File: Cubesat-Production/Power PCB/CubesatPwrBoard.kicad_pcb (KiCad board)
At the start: 2 copper layers, 90 x 96 mm, 57 parts, among them J1 SystemLoad, J10 Test_Point, J11 Test_Point, J14 Test_Point, J15 Test_Point, J16 Test_Point_GND, J2 SystemLoad, J3 I2C, J6 Test_Point, J7 Test_Point, Q1 TQM110NB04CR_RLG, Q2 2N7002*, U1 LTC4162

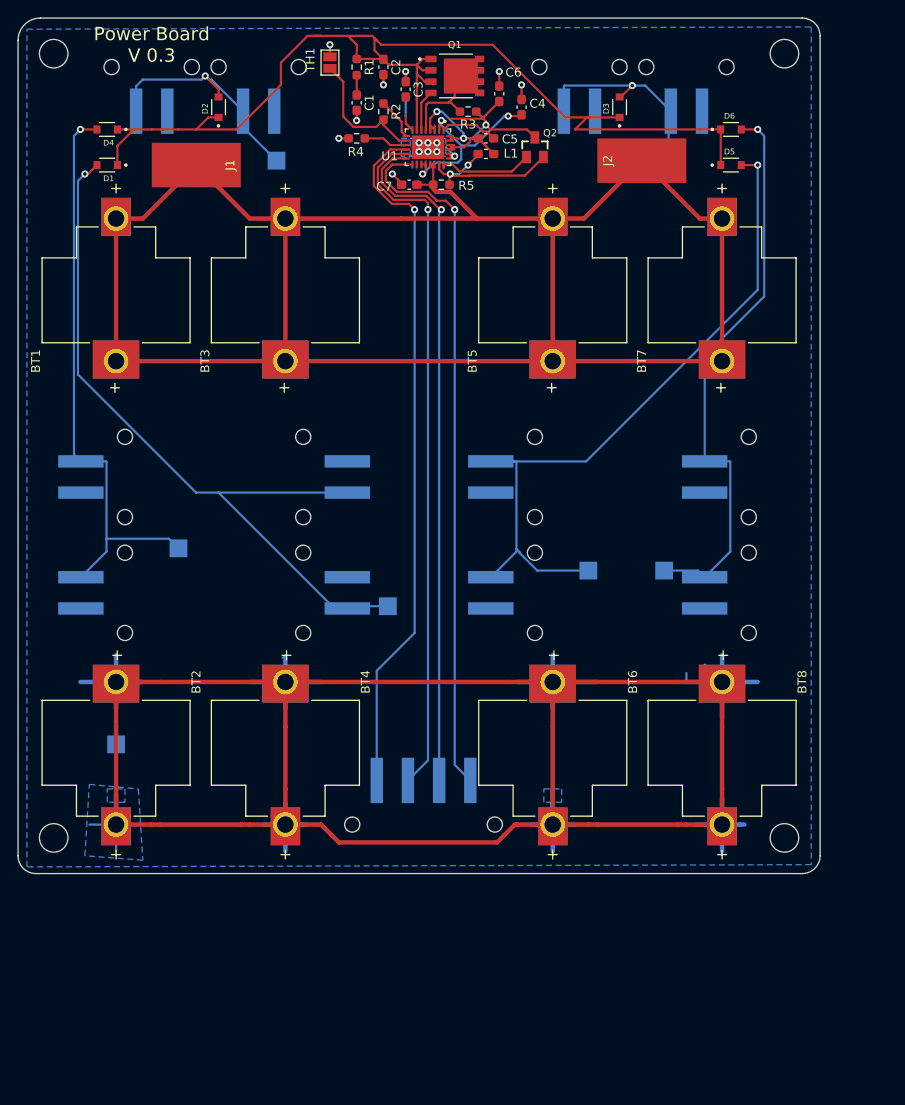
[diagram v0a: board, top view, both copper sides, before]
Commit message: copies current-revision to production branch
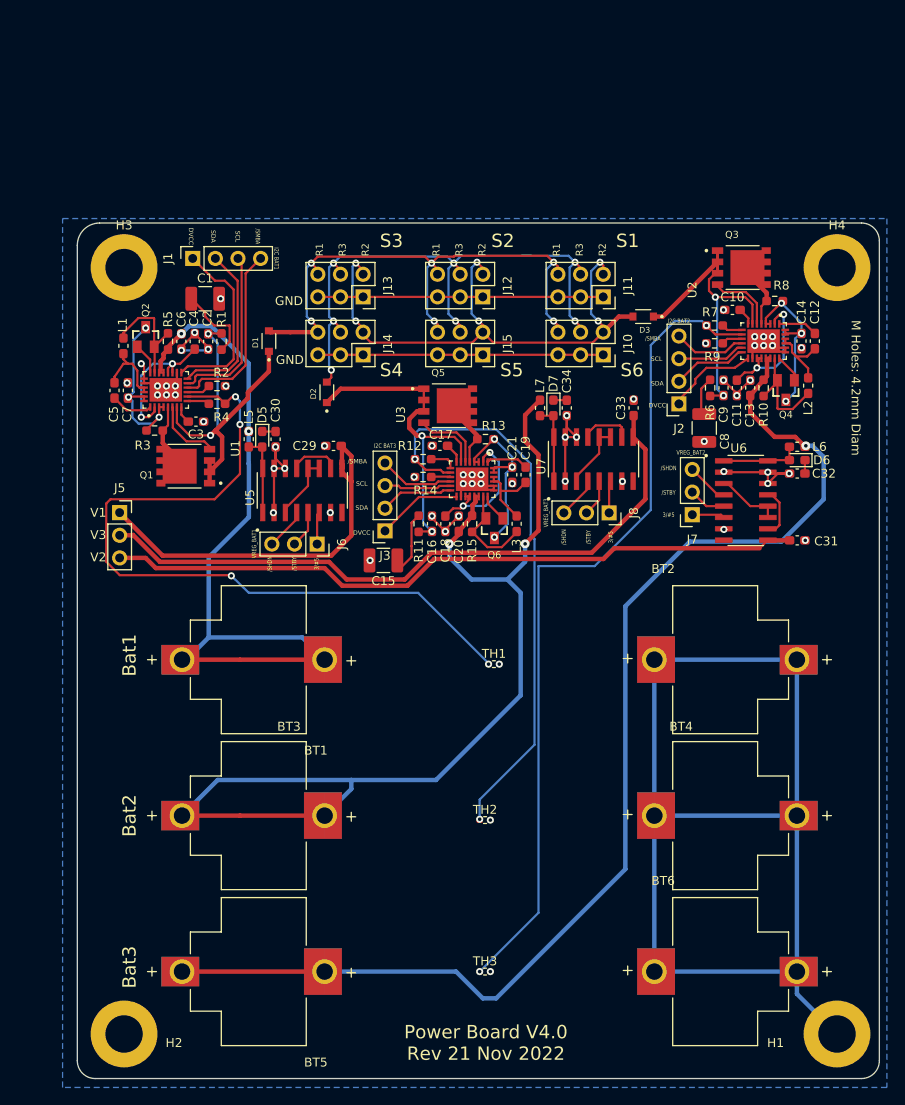
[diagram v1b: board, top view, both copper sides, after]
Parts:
- removed BT7, BT8: 254TR, 254TR:BAT_254TR
- removed D4: D_Schottky_Small, CUS520,H3F:DIO_CUS520,H3F
- removed J16: Test_Point_GND, TestPoint:TestPoint_Pad_2.0x2.0mm
- removed REF** (x4): MountingHole_3.2mm_M3, MountingHole:MountingHole_3.2mm_M3
- removed SC1, SC10, SC11, SC12, SC2, SC3, SC4, SC5, SC6, SC7, SC8, SC9: Solar_Cells, 6915_1x2:691508110302
- added C10: 1u, Capacitor_SMD:C_0603_1608Metric_Pad1.08x0.95mm_HandSolder, F.Cu at (180.2, 55.2)
- added C11: 4.7u, Capacitor_SMD:C_0603_1608Metric_Pad1.08x0.95mm_HandSolder, F.Cu at (180.7, 64.0)
- added C12: C, Capacitor_SMD:C_0603_1608Metric_Pad1.08x0.95mm_HandSolder, F.Cu at (189.4, 58.8)
- added C13: 10u, Capacitor_SMD:C_0603_1608Metric_Pad1.08x0.95mm_HandSolder, F.Cu at (182.2, 64.0)
- added C14: 10u, Capacitor_SMD:C_0603_1608Metric_Pad1.08x0.95mm_HandSolder, F.Cu at (187.9, 58.8)
- added C15: 150u, Capacitor_SMD:C_1210_3225Metric_Pad1.33x2.70mm_HandSolder, F.Cu at (141.0, 83.4)
- added C16: C_Polarized_US, Capacitor_SMD:C_0603_1608Metric_Pad1.08x0.95mm_HandSolder, F.Cu at (146.5, 79.2)
- added C17: 1u, Capacitor_SMD:C_0603_1608Metric_Pad1.08x0.95mm_HandSolder, F.Cu at (147.3, 70.5)
- added C18: 4.7u, Capacitor_SMD:C_0603_1608Metric_Pad1.08x0.95mm_HandSolder, F.Cu at (148.0, 79.2)
- added C19: C, Capacitor_SMD:C_0603_1608Metric_Pad1.08x0.95mm_HandSolder, F.Cu at (157.0, 73.8)
- added C20: 10u, Capacitor_SMD:C_0603_1608Metric_Pad1.08x0.95mm_HandSolder, F.Cu at (149.5, 79.2)
- added C21: 10u, Capacitor_SMD:C_0603_1608Metric_Pad1.08x0.95mm_HandSolder, F.Cu at (155.5, 73.8)
- added C29: C_Polarized_US, Capacitor_SMD:C_0603_1608Metric_Pad1.08x0.95mm_HandSolder, F.Cu at (135.4, 70.5)
- added C30: C_Polarized_US, Capacitor_SMD:C_0603_1608Metric_Pad1.08x0.95mm_HandSolder, F.Cu at (128.9, 69.8)
- added C31: 4.7u, Capacitor_SMD:C_0603_1608Metric_Pad1.08x0.95mm_HandSolder, F.Cu at (187.4, 81.1)
- added C32: 100u, Capacitor_SMD:C_0603_1608Metric_Pad1.08x0.95mm_HandSolder, F.Cu at (187.4, 73.6)
- added C33: 4.7u, Capacitor_SMD:C_0603_1608Metric_Pad1.08x0.95mm_HandSolder, F.Cu at (169.1, 66.2)
- added C34: 100u, Capacitor_SMD:C_0603_1608Metric_Pad1.08x0.95mm_HandSolder, F.Cu at (161.6, 66.2)
- added C8: 150u, Capacitor_SMD:C_1210_3225Metric_Pad1.33x2.70mm_HandSolder, F.Cu at (177.0, 68.5)
- added C9: C_Polarized_US, Capacitor_SMD:C_0603_1608Metric_Pad1.08x0.95mm_HandSolder, F.Cu at (179.2, 64.0)
- added D7: D_Schottky, Diode_SMD:D_0603_1608Metric_Pad1.05x0.95mm_HandSolder, F.Cu at (160.1, 66.2)
- added H1: MountingHole_Pad, MountingHole:MountingHole_4.3mm_M4_DIN965_Pad, F.Cu at (191.9, 136.5)
- added H2: MountingHole_Pad, MountingHole:MountingHole_4.3mm_M4_DIN965_Pad, F.Cu at (111.9, 136.5)
- added H3: MountingHole_Pad, MountingHole:MountingHole_4.3mm_M4_DIN965_Pad, F.Cu at (111.9, 50.5)
- added H4: MountingHole_Pad, MountingHole:MountingHole_4.3mm_M4_DIN965_Pad, F.Cu at (191.9, 50.5)
- added J12: S3, Connector_PinSocket_2.54mm:PinSocket_2x03_P2.54mm_Vertical, F.Cu at (152.2, 53.8)
- added J13: S4, Connector_PinSocket_2.54mm:PinSocket_2x03_P2.54mm_Vertical, F.Cu at (138.7, 53.8)
- added J5: Conn_01x04_Female, Connector_PinSocket_2.54mm:PinSocket_1x03_P2.54mm_Vertical, F.Cu at (111.4, 78.0)
- added J8: Conn_01x03_Female, Connector_PinSocket_2.54mm:PinSocket_1x03_P2.54mm_Vertical, F.Cu at (166.3, 78.0)
- added L2: 4.7u, Inductor_SMD:L_0603_1608Metric_Pad1.05x0.95mm_HandSolder, F.Cu at (188.7, 63.8)
- added L3: 4.7u, Inductor_SMD:L_0603_1608Metric_Pad1.05x0.95mm_HandSolder, F.Cu at (156.0, 79.2)
- added L5: L, Inductor_SMD:L_0603_1608Metric_Pad1.05x0.95mm_HandSolder, F.Cu at (125.9, 69.8)
- added L6: 22u, Inductor_SMD:L_0603_1608Metric_Pad1.05x0.95mm_HandSolder, F.Cu at (187.4, 70.6)
- added L7: 22u, Inductor_SMD:L_0603_1608Metric_Pad1.05x0.95mm_HandSolder, F.Cu at (158.6, 66.2)
- added Q3: TQM110NB04CR_RLG, TQM110N:TRANS_TQM110NB04CR_RLG, F.Cu at (181.2, 50.5)
- added Q4: 2N7002*, 2N7002:SOT23, F.Cu at (186.2, 64.2)
- added Q5: TQM110NB04CR_RLG, TQM110N:TRANS_TQM110NB04CR_RLG, F.Cu at (148.2, 66.0)
- added Q6: 2N7002*, 2N7002:SOT23, F.Cu at (153.5, 79.8)
- added R10: 10m, Resistor_SMD:R_0603_1608Metric_Pad0.98x0.95mm_HandSolder, F.Cu at (183.7, 64.0)
- added R11: 2.5, Resistor_SMD:R_0603_1608Metric_Pad0.98x0.95mm_HandSolder, F.Cu at (145.0, 79.2)
- added R12: 16m, Resistor_SMD:R_0603_1608Metric_Pad0.98x0.95mm_HandSolder, F.Cu at (145.5, 72.0)
- added R13: 16m, Resistor_SMD:R_0603_1608Metric_Pad0.98x0.95mm_HandSolder, F.Cu at (152.5, 69.8)
- added R14: 63.4k, Resistor_SMD:R_0603_1608Metric_Pad0.98x0.95mm_HandSolder, F.Cu at (145.5, 74.0)
- added R15: 10m, Resistor_SMD:R_0603_1608Metric_Pad0.98x0.95mm_HandSolder, F.Cu at (151.0, 79.2)
- added R6: 2.5, Resistor_SMD:R_0603_1608Metric_Pad0.98x0.95mm_HandSolder, F.Cu at (177.7, 64.0)
- added R7: 16m, Resistor_SMD:R_0603_1608Metric_Pad0.98x0.95mm_HandSolder, F.Cu at (178.2, 57.0)
- added R8: 16m, Resistor_SMD:R_0603_1608Metric_Pad0.98x0.95mm_HandSolder, F.Cu at (184.9, 54.2)
- added R9: 63.4k, Resistor_SMD:R_0603_1608Metric_Pad0.98x0.95mm_HandSolder, F.Cu at (178.2, 59.0)
- added TH2: Thermistor_NTC, Resistor_SMD:R_0402_1005Metric_Pad0.72x0.64mm_HandSolder, F.Cu at (152.4, 112.5)
- added TH3: Thermistor_NTC, Resistor_SMD:R_0402_1005Metric_Pad0.72x0.64mm_HandSolder, F.Cu at (152.4, 129.5)
- added U2: LTC4162, LTC4162:QFN50P500X400X80-29N, F.Cu at (183.7, 58.8)
- added U3: LTC4162, LTC4162:QFN50P500X400X80-29N, F.Cu at (151.0, 74.2)
- added U5: MAX710ESE+T, MAX710ESE:SOIC127P600X175-16N, F.Cu at (131.9, 75.5)
- added U6: MAX710ESE+T, MAX710ESE:SOIC127P600X175-16N, F.Cu at (181.7, 76.6)
- added U7: MAX710ESE+T, MAX710ESE:SOIC127P600X175-16N, F.Cu at (164.6, 72.0)
- C1: value 150u -> C_Polarized_US; footprint Capacitor_SMD:C_0603_1608Metric_Pad1.08x0.95mm_HandSolder -> Capacitor_SMD:C_1210_3225Metric_Pad1.33x2.70mm_HandSolder
- C2: value 0.1u -> C_Polarized_US
- C3: value 1u -> C
- C4: value 4.7u -> C
- C5: value 22n -> C
- C6, C7: value 10u -> C
- D5, D6: value D_Schottky_Small -> D_Schottky; footprint CUS520,H3F:DIO_CUS520,H3F -> Diode_SMD:D_0603_1608Metric_Pad1.05x0.95mm_HandSolder
- J1, J2: value SystemLoad -> Conn_01x04_Female; footprint Connector_Wire:SolderWirePad_1x01_SMD_5x10mm -> Connector_PinSocket_2.54mm:PinSocket_1x04_P2.54mm_Vertical
- J10: value Test_Point -> S1; footprint TestPoint:TestPoint_Pad_2.0x2.0mm -> Connector_PinSocket_2.54mm:PinSocket_2x03_P2.54mm_Vertical; moved to F.Cu
- J11: value Test_Point -> S2; footprint TestPoint:TestPoint_Pad_2.0x2.0mm -> Connector_PinSocket_2.54mm:PinSocket_2x03_P2.54mm_Vertical; moved to F.Cu
- J14: value Test_Point -> S5; footprint TestPoint:TestPoint_Pad_2.0x2.0mm -> Connector_PinSocket_2.54mm:PinSocket_2x03_P2.54mm_Vertical; moved to F.Cu
- J15: value Test_Point -> S6; footprint TestPoint:TestPoint_Pad_2.0x2.0mm -> Connector_PinSocket_2.54mm:PinSocket_2x03_P2.54mm_Vertical; moved to F.Cu
- J3: value I2C -> Conn_01x04_Female; footprint 6915_1x4:691508110304 -> Connector_PinSocket_2.54mm:PinSocket_1x04_P2.54mm_Vertical; moved to F.Cu
- J6, J7: value Test_Point -> Conn_01x03_Female; footprint TestPoint:TestPoint_Pad_2.0x2.0mm -> Connector_PinSocket_2.54mm:PinSocket_1x03_P2.54mm_Vertical; moved to F.Cu
- L1: value 4.7u -> L
- R1: value 2.5 -> R
- R2, R3: value 16m -> R
- R4: value 63.4k -> R
- R5: value 10m -> R
- TH1: footprint Jumper:SolderJumper-2_P1.3mm_Open_Pad1.0x1.5mm -> Resistor_SMD:R_0402_1005Metric_Pad0.72x0.64mm_HandSolder
- moved BT5 83.6 mm to (126.4, 129.5), turned to 180 degrees
- moved TH1 70.0 mm to (153.4, 95.0), turned to 0 degrees
- moved BT2 69.2 mm to (179.4, 94.5), turned to 0 degrees
- moved J7 61.3 mm to (175.7, 78.2), turned to 180 degrees
- moved D5 60.9 mm to (127.4, 69.8), turned to -90 degrees
- moved BT3 59.1 mm to (126.4, 112.0), turned to 180 degrees
- moved J11 55.4 mm to (165.7, 53.8), turned to -90 degrees
- moved Q1 53.2 mm to (118.8, 72.8), turned to 180 degrees
- moved C5 50.4 mm to (110.8, 64.3), turned to 90 degrees
- moved R3 50.2 mm to (115.3, 68.8), turned to 0 degrees
- moved BT4 49.9 mm to (179.4, 112.0), turned to 0 degrees
- moved Q2 48.6 mm to (114.3, 58.3)
- moved L1 46.0 mm to (111.8, 59.3), turned to 90 degrees
- moved C6 45.2 mm to (118.3, 58.8), turned to -90 degrees
- moved C4 45.1 mm to (119.8, 58.8)
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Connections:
- net Net-(R2-Pad2) renamed /Bat_Reg_1/TH
- BT1 pad P1_1: Net-(BT1-PadP1_1) -> /Bat_Reg_1/V_Bat
- BT1 pad P1_2: Net-(BT1-PadP1_1) -> /Bat_Reg_1/V_Bat
- BT3 pad P1_1: Net-(BT1-PadP1_1) -> /Bat_Reg_2/V_Bat
- BT3 pad P1_2: Net-(BT1-PadP1_1) -> /Bat_Reg_2/V_Bat
- BT5 pad P1_1: Net-(BT1-PadP1_1) -> /Bat_Reg_3/V_Bat
- BT5 pad P1_2: Net-(BT1-PadP1_1) -> /Bat_Reg_3/V_Bat
- C2 pad 1: Net-(C2-Pad1) -> /Bat_Reg_1/VIN
- C6 pad 1: Net-(C6-Pad1) -> /Bat_Reg_1/V_Bat
- C7 pad 1: Net-(BT1-PadP1_1) -> Net-(C7-Pad1)
- D1 pad 1: Net-(C2-Pad1) -> /Bat_Reg_1/VIN
- D2 pad 1: Net-(C2-Pad1) -> /Bat_Reg_2/VIN
- D3 pad 1: Net-(C2-Pad1) -> /Bat_Reg_3/VIN
- D5 pad 1: Net-(C2-Pad1) -> Net-(C30-Pad1)
- D6 pad 1: Net-(C2-Pad1) -> Net-(C32-Pad1)
- J1 pad 1: Net-(BT1-PadP1_1) -> /Bat_Reg_1/DVCC
- J10 pad 1: Net-(D3-Pad2) -> GND
- J11 pad 1: Net-(D4-Pad2) -> GND
- J14 pad 1: Net-(D5-Pad2) -> GND
- J15 pad 1: Net-(D6-Pad2) -> GND
- J2 pad 1: Net-(BT1-PadP1_1) -> /Bat_Reg_3/DVCC
- J3 pad 1: Net-(J3-Pad1) -> /Bat_Reg_2/DVCC
- J3 pad 2: Net-(J3-Pad2) -> /Bat_Reg_2/SDA
- J3 pad 3: Net-(J3-Pad3) -> /Bat_Reg_2/SCL
- J3 pad 4: Net-(J3-Pad4) -> /Bat_Reg_2//SMBALERT
- J6 pad 1: Net-(D1-Pad2) -> /V_Reg_3.3_5V1/3/#5
- J7 pad 1: Net-(D2-Pad2) -> /V_Reg_3.3_5V3/3/#5
- Q1 pad 1: Net-(C2-Pad1) -> /Bat_Reg_1/VIN
- Q1 pad 2: Net-(C2-Pad1) -> /Bat_Reg_1/VIN
- Q1 pad 3: Net-(C2-Pad1) -> /Bat_Reg_1/VIN
- Q2 pad 3: Net-(C6-Pad1) -> Net-(C7-Pad1)
- R1 pad 1: Net-(C2-Pad1) -> /Bat_Reg_1/VIN
- R3 pad 1: Net-(C6-Pad1) -> Net-(C7-Pad1)
- R5 pad 1: Net-(BT1-PadP1_1) -> /Bat_Reg_1/V_Bat
- U1 pad 12: Net-(J3-Pad4) -> /Bat_Reg_1//SMBALERT
- U1 pad 13: Net-(J3-Pad3) -> /Bat_Reg_1/SCL
- U1 pad 14: Net-(J3-Pad2) -> /Bat_Reg_1/SDA
- U1 pad 15: Net-(J3-Pad1) -> /Bat_Reg_1/DVCC
- U1 pad 19: Net-(BT1-PadP1_1) -> /Bat_Reg_1/V_Bat
- U1 pad 20: Net-(BT1-PadP1_1) -> /Bat_Reg_1/V_Bat
- U1 pad 27: Net-(C6-Pad1) -> Net-(C7-Pad1)
- U1 pad 28: Net-(C6-Pad1) -> Net-(C7-Pad1)
- U1 pad 3: Net-(C6-Pad1) -> Net-(C7-Pad1)
- U1 pad 4: Net-(C6-Pad1) -> Net-(C7-Pad1)
- U1 pad 7: Net-(C2-Pad1) -> /Bat_Reg_1/VIN
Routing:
- net Net-(BT1-PadP1_1): track 221.8 -> 0.00 mm
- net /Bat_Reg_3/V_Bat: track 0.00 -> 136.4 mm, vias 0 -> 1
- net Net-(C2-Pad1): track 123.7 -> 0.00 mm
- net /Bat_Reg_2/V_Bat: track 0.00 -> 117.6 mm, vias 0 -> 2
- net /Bat_Reg_3/TH: track 0.00 -> 93.9 mm, vias 0 -> 2
- net /Bat_Reg_1/V_Bat: track 0.00 -> 81.9 mm, vias 0 -> 2
- net /V_Reg_3.3_5V3/Vout: track 0.00 -> 78.6 mm
- net Net-(J3-Pad1): track 78.2 -> 0.00 mm, vias 1 -> 0
- net Net-(J3-Pad4): track 78.1 -> 0.00 mm, vias 1 -> 0
- net Net-(J3-Pad3): track 77.9 -> 0.00 mm, vias 1 -> 0
- net Net-(J3-Pad2): track 76.8 -> 0.00 mm, vias 1 -> 0
- net /V_Reg_3.3_5V2/Vout: track 0.00 -> 74.8 mm
- net Net-(D5-Pad2): track 79.9 -> 8.89 mm, vias 1 -> 0
- net /Bat_Reg_1/TH: track 15.6 -> 85.6 mm, vias 0 -> 4
- net Net-(D4-Pad2): track 65.3 -> 0.00 mm, vias 1 -> 0
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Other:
- net class Battery removed
- net class Default removed
- board text added: "/SHDN"
- board text added: "/SMBA"
- board text added: "/STBY"
- board text added: "3/#5"
- board text added: "Bat1"
- board text added: "Bat2"
- board text added: "Bat3"
- board text added: "DVCC"
- board text added: "GND"
- board text added: "I2C BAT1"
- board text added: "I2C BAT2"
- board text added: "I2C BAT3"
- board text added: "M Holes: 4.2mm Diam"
- board text added: "Power Board V4.0 Rev 21 Nov 2022"
- board text added: "R1 R3 R2"
- board text added: "S1"
- board text added: "S2"
- board text added: "S3"
- board text added: "S4"
- board text added: "S5"
- board text added: "S6"
- board text added: "SCL"
- board text added: "SDA"
- board text added: "V1"
- board text added: "V2"
- board text added: "V3"
- board text added: "VREG_BAT1"
- board text added: "VREG_BAT2"
- board text added: "VREG_BAT3"
- board text removed: "I2C"
- board text removed: "Power Board V 0.3"
- board text removed: "SIDE 1"
- board text removed: "SIDE 2"
- board text removed: "SIDE 3"
- board text removed: "SIDE 4"
- board text removed: "SIDE 5"
- board text removed: "SIDE 6"
